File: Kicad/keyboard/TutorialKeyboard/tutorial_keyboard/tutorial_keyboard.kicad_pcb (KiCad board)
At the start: 2 copper layers, 113 parts, among them J1 USB_C_Receptacle_USB2.0, K1 KEYSW, K10 KEYSW, K11 KEYSW, K12 KEYSW, K13 KEYSW, K14 KEYSW, K15 KEYSW, K16 KEYSW, K17 KEYSW, K18 KEYSW, K19 KEYSW, K2 KEYSW, K20 KEYSW, K21 KEYSW, K22 KEYSW, K23 KEYSW, K24 KEYSW, K25 KEYSW, K26 KEYSW, K27 KEYSW, K28 KEYSW, K29 KEYSW, K3 KEYSW, K30 KEYSW, K31 KEYSW, K32 KEYSW, K33 KEYSW, K34 KEYSW, K35 KEYSW, K36 KEYSW, K37 KEYSW, K38 KEYSW, K39 KEYSW, K4 KEYSW, K40 KEYSW, K41 KEYSW, K42 KEYSW, K43 KEYSW, K44 KEYSW, K45 KEYSW, K46 KEYSW, K47 KEYSW, K5 KEYSW, K6 KEYSW, K7 KEYSW, K8 KEYSW, K9 KEYSW, SW1 SW_PUSH, U1 ATMEGA32U4, X1 XTAL

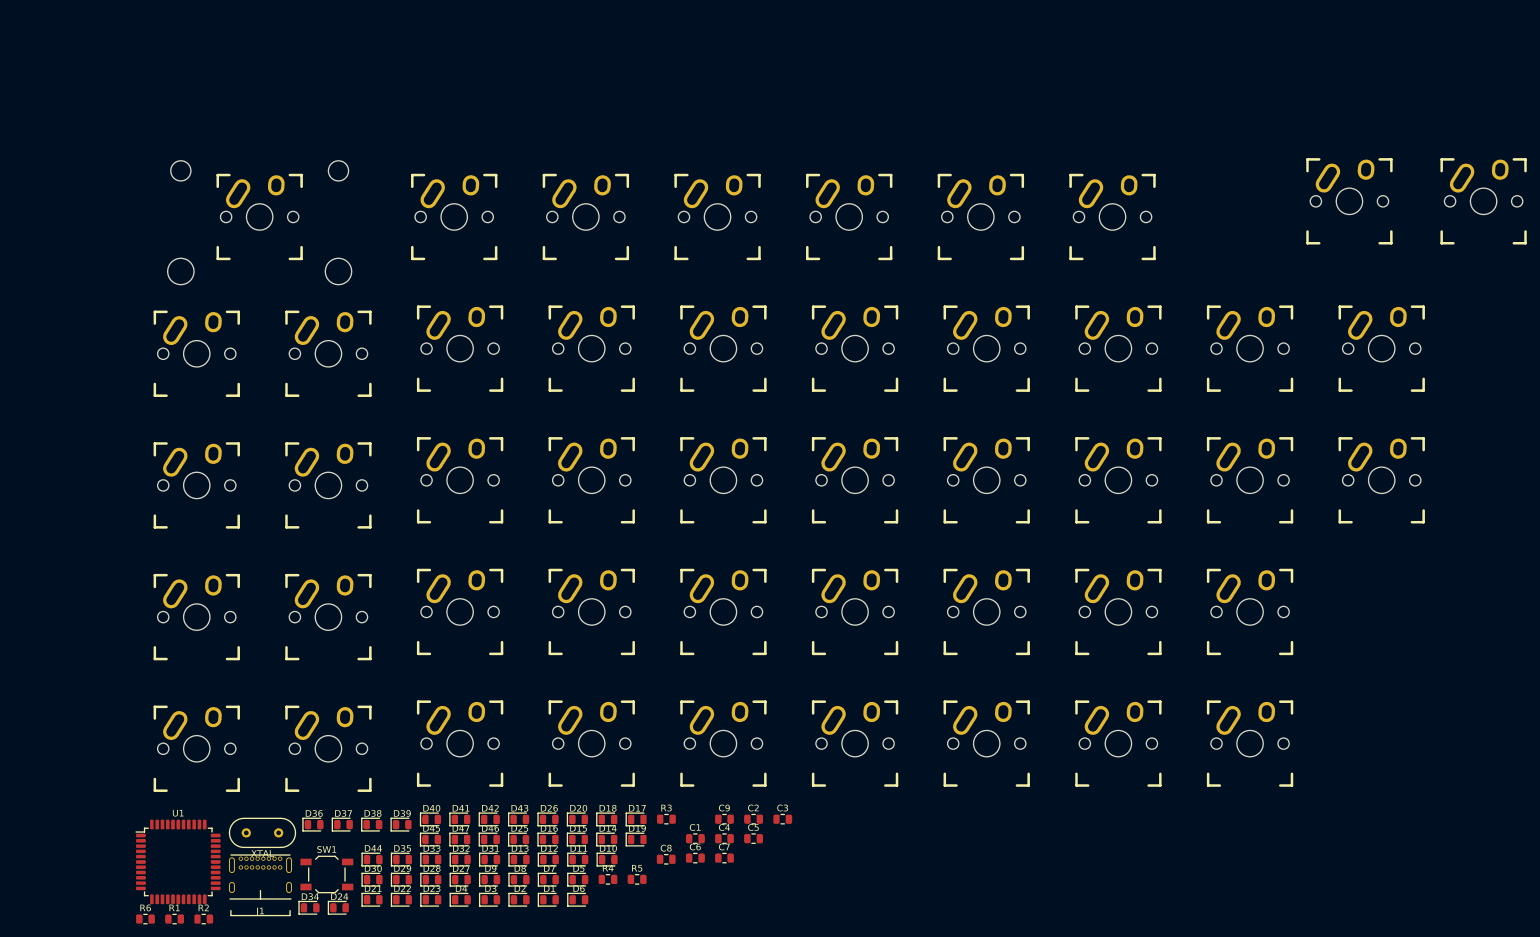
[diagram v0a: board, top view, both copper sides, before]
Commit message: up to routing section
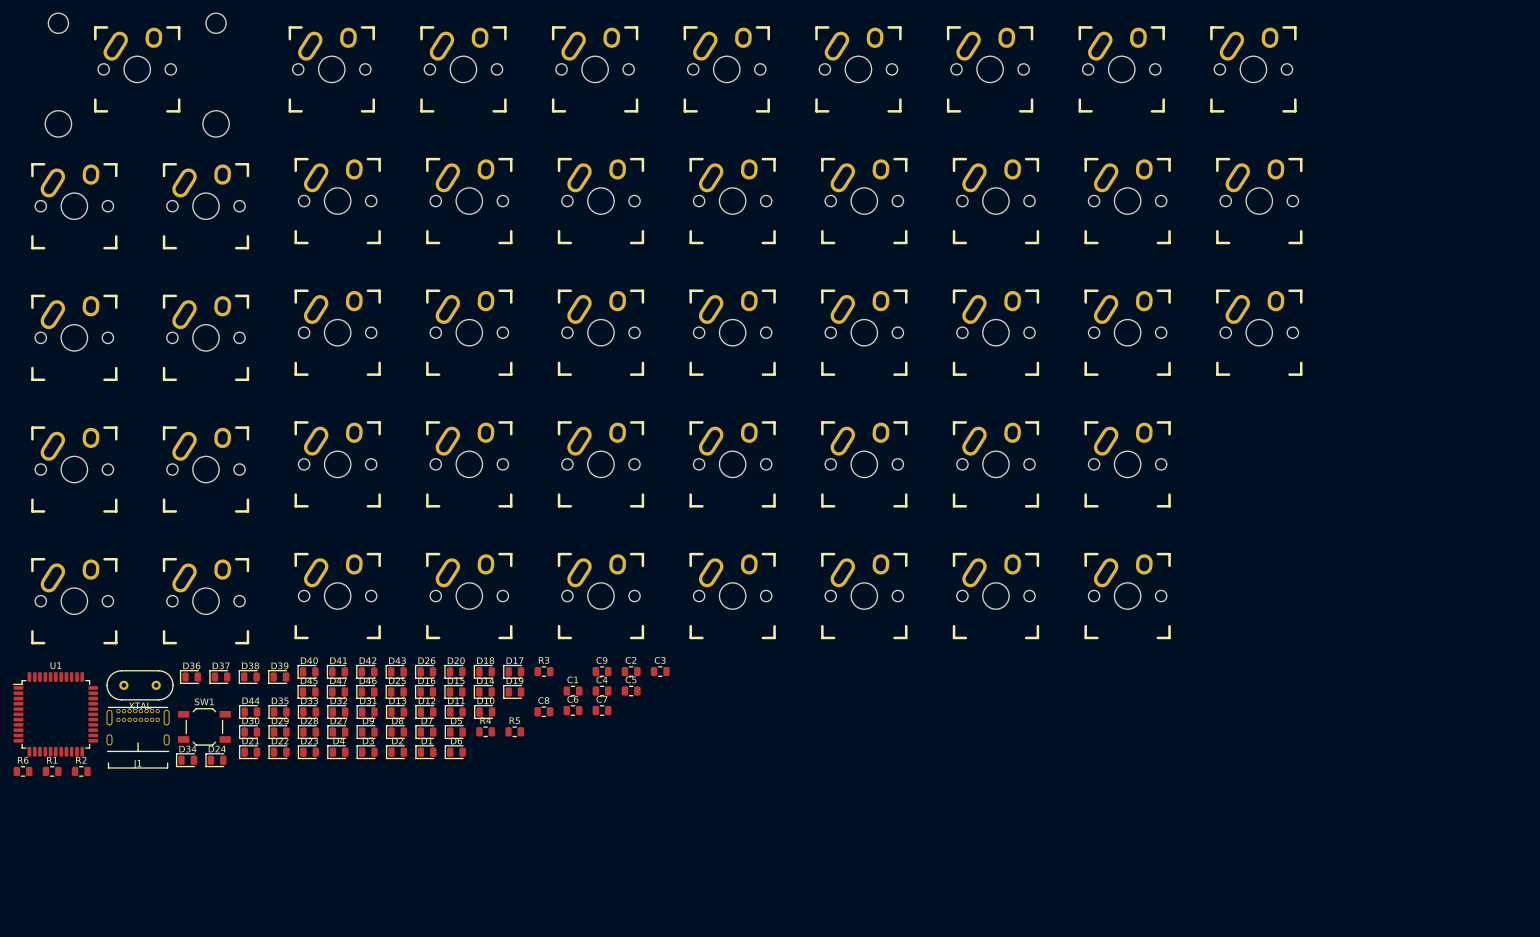
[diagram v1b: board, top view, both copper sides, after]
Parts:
- moved K19 40.2 mm to (201.4, 25.7)
- moved K24 39.9 mm to (181.4, 25.7)
- moved D27 29.0 mm to (62.9, 126.1)
- moved D28 29.0 mm to (58.4, 126.1)
- moved D29 29.0 mm to (54.0, 126.1)
- moved D5 29.0 mm to (80.7, 126.1)
- moved D7 29.0 mm to (76.2, 126.1)
- moved D8 29.0 mm to (71.8, 126.1)
- moved D30 29.0 mm to (49.5, 126.1)
- moved C1 29.0 mm to (98.3, 119.9)
- moved C4 29.0 mm to (102.7, 119.9)
- moved C5 29.0 mm to (107.1, 119.9)
- moved C6 29.0 mm to (98.3, 122.8)
- moved C7 29.0 mm to (102.7, 122.8)
- moved C8 29.0 mm to (93.9, 123.0)
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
